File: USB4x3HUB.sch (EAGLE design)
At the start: 119 parts, among them IC1 TUSB2036, IC10 SN74LVC1G139DCTR, IC2 FSUSB74MPX, IC3 TPS2041C, IC4 TPS2041C, IC5 TPS2041C, IC6 3.3V, IC7 5V, IC8 5V, IC9 5V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

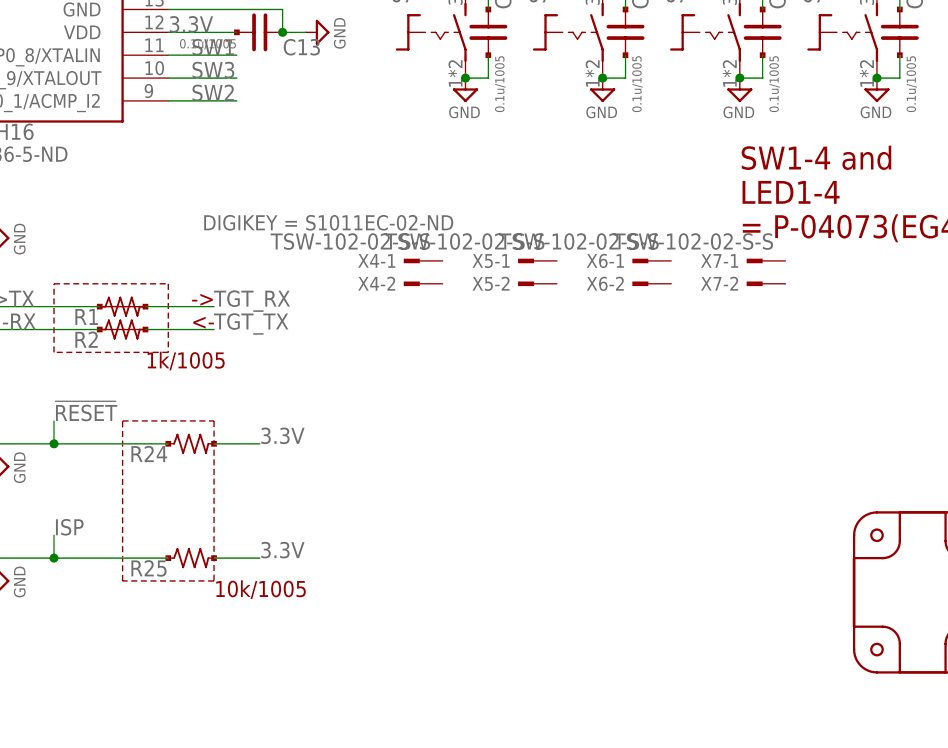
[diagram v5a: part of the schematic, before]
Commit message: [ BRD ] X4-7 pin1 connects to each switch inputs
- move SW1-4 silk
- move CON1-4 silk
- move X4-7 silk
- add 2.8mm hole for M2.6 screw
   - add tRestrict zone for it
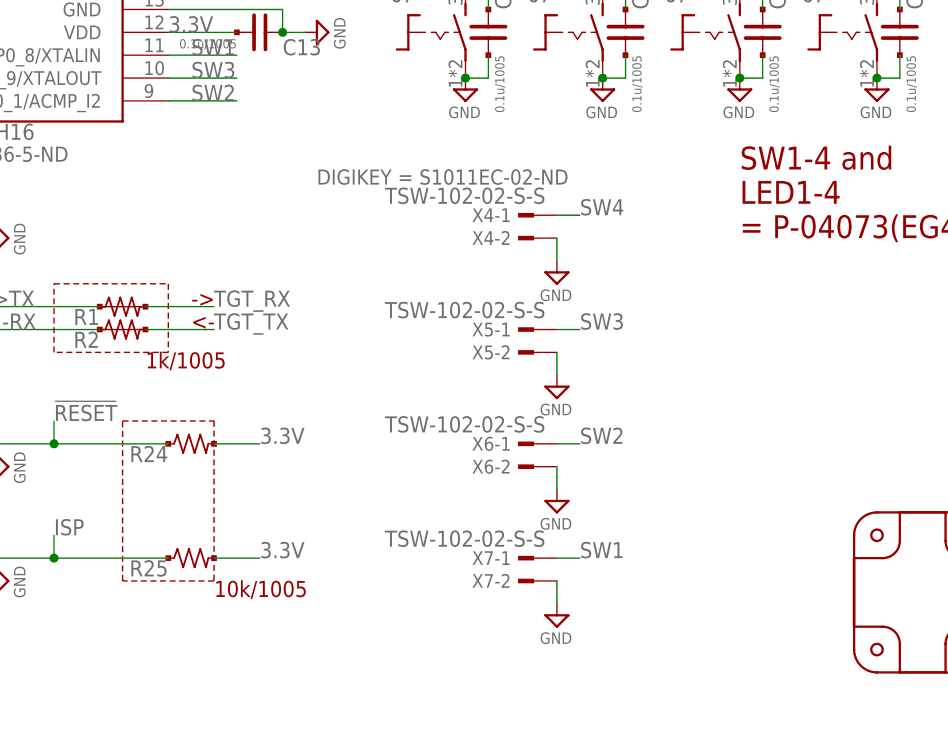
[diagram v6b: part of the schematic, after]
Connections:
- net GND: now also X4-2.1, X5-2.1, X6-2.1, X7-2.1
- net SW1: now also X7-1.1
- net SW2: now also X6-1.1
- net SW3: now also X5-1.1
- net SW4: now also X4-1.1
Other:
- moved on the sheet: X4-1, X4-2, X5-1, X5-2, X6-1, X6-2, X7-1, X7-2
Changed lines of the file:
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@@
 <part name="SW2" library="mylib" deviceset="TACTSW2_*" device="_SKRPACE010" technology="WH"/>
 <part name="SW1" library="mylib" deviceset="TACTSW2_*" device="_SKRPACE010" technology="WH"/>
+<part name="SUPPLY34" library="mylib" deviceset="GND" device=""/>
+<part name="SUPPLY42" library="mylib" deviceset="GND" device=""/>
+<part name="SUPPLY43" library="mylib" deviceset="GND" device=""/>
+<part name="SUPPLY44" library="mylib" deviceset="GND" device=""/>
 </parts>
 <sheets>
@@
 <instance part="P4" gate="G$1" x="251.46" y="10.16"/>
 <instance part="TP5" gate="1" x="165.1" y="157.48" rot="R180"/>
-<instance part="X4" gate="-1" x="193.04" y="50.8" rot="MR0">
-<attribute name="DIGIKEY" x="182.88" y="55.88" size="1.6764" layer="96" rot="MR180" align="bottom-center" display="both"/>
-</instance>
-<instance part="X4" gate="-2" x="193.04" y="48.26" rot="MR0"/>
-<instance part="X5" gate="-1" x="205.74" y="50.8" rot="MR0"/>
-<instance part="X5" gate="-2" x="205.74" y="48.26" rot="MR0"/>
-<instance part="X6" gate="-1" x="218.44" y="50.8" rot="MR0"/>
-<instance part="X6" gate="-2" x="218.44" y="48.26" rot="MR0"/>
-<instance part="X7" gate="-1" x="231.14" y="50.8" rot="MR0"/>
-<instance part="X7" gate="-2" x="231.14" y="48.26" rot="MR0"/>
+<instance part="X4" gate="-1" x="205.74" y="55.88" rot="MR0">
+<attribute name="DIGIKEY" x="195.58" y="60.96" size="1.6764" layer="96" rot="MR180" align="bottom-center" display="both"/>
+</instance>
+<instance part="X4" gate="-2" x="205.74" y="53.34" rot="MR0"/>
+<instance part="X5" gate="-1" x="205.74" y="43.18" rot="MR0"/>
+<instance part="X5" gate="-2" x="205.74" y="40.64" rot="MR0"/>
+<instance part="X6" gate="-1" x="205.74" y="30.48" rot="MR0"/>
+<instance part="X6" gate="-2" x="205.74" y="27.94" rot="MR0"/>
+<instance part="X7" gate="-1" x="205.74" y="17.78" rot="MR0"/>
+<instance part="X7" gate="-2" x="205.74" y="15.24" rot="MR0"/>
 <instance part="SW4" gate="G$1" x="195.58" y="76.2"/>
 <instance part="SW3" gate="G$1" x="210.82" y="76.2"/>
 <instance part="SW2" gate="G$1" x="226.06" y="76.2"/>
 <instance part="SW1" gate="G$1" x="241.3" y="76.2"/>
+<instance part="SUPPLY34" gate="GND" x="208.28" y="48.26"/>
+<instance part="SUPPLY42" gate="GND" x="208.28" y="35.56"/>
+<instance part="SUPPLY43" gate="GND" x="208.28" y="22.86"/>
+<instance part="SUPPLY44" gate="GND" x="208.28" y="10.16"/>
 </instances>
 <busses>
@@
 <pinref part="SUPPLY41" gate="GND" pin="GND"/>
 </segment>
+<segment>
+<pinref part="X4" gate="-2" pin="1"/>
+<pinref part="SUPPLY34" gate="GND" pin="GND"/>
+<wire x1="208.28" y1="50.8" x2="208.28" y2="53.34" width="0.1524" layer="91"/>
+</segment>
+<segment>
+<pinref part="X5" gate="-2" pin="1"/>
+<pinref part="SUPPLY42" gate="GND" pin="GND"/>
+<wire x1="208.28" y1="38.1" x2="208.28" y2="40.64" width="0.1524" layer="91"/>
+</segment>
+<segment>
+<pinref part="X6" gate="-2" pin="1"/>
+<pinref part="SUPPLY43" gate="GND" pin="GND"/>
+<wire x1="208.28" y1="25.4" x2="208.28" y2="27.94" width="0.1524" layer="91"/>
+</segment>
+<segment>
+<pinref part="X7" gate="-2" pin="1"/>
+<pinref part="SUPPLY44" gate="GND" pin="GND"/>
+<wire x1="208.28" y1="12.7" x2="208.28" y2="15.24" width="0.1524" layer="91"/>
+</segment>
 </net>
 <net name="3.3V" class="0">
@@
 <label x="167.64" y="73.66" size="1.778" layer="95"/>
 </segment>
+<segment>
+<wire x1="208.28" y1="17.78" x2="210.82" y2="17.78" width="0.1524" layer="91"/>
+<pinref part="X7" gate="-1" pin="1"/>
+<label x="210.82" y="17.78" size="1.778" layer="95"/>
+</segment>
 </net>
 <net name="SW2" class="0">
@@
 <label x="167.64" y="68.58" size="1.778" layer="95"/>
 </segment>
+<segment>
+<wire x1="208.28" y1="30.48" x2="210.82" y2="30.48" width="0.1524" layer="91"/>
+<pinref part="X6" gate="-1" pin="1"/>
+<label x="210.82" y="30.48" size="1.778" layer="95"/>
+</segment>
 </net>
 <net name="SW3" class="0">
@@
 <label x="167.64" y="71.12" size="1.778" layer="95"/>
 </segment>
+<segment>
+<wire x1="208.28" y1="43.18" x2="210.82" y2="43.18" width="0.1524" layer="91"/>
+<pinref part="X5" gate="-1" pin="1"/>
+<label x="210.82" y="43.18" size="1.778" layer="95"/>
+</segment>
 </net>
 <net name="SW4" class="0">
@@
 <label x="106.68" y="68.58" size="1.778" layer="95"/>
 </segment>
-</net>
+<segment>
+<wire x1="208.28" y1="55.88" x2="210.82" y2="55.88" width="0.1524" layer="91"/>
+<pinref part="X4" gate="-1" pin="1"/>
+<label x="210.82" y="55.88" size="1.778" layer="95"/>
+</segment>
+</net>

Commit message: [ PCB ] add sheet for daughter board; move M2.6 hole; library update
- prepare daughter board
- apply updated library and use TACTSW2 component
- more consideration required
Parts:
- added P5, P6, P7, P8: (no value), mylib:PCB_CORNER_NH
- added SW5, SW6, SW7, SW8: (no value), mylib:TACTSW2_BK_TL1105S
- added X10, X11, X8, X9: TSW-102-02-S-S, con-samtec.local:TSW-102-02-S-S
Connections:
- new net N$74: SW8.S, X8-2.1
- new net N$75: SW7.S, X9-2.1
- new net N$76: SW6.S, X10-2.1
- new net N$77: SW5.S, X11-2.1
- new net SW5: SW5.P, X11-1.1
- new net SW6: SW6.P, X10-1.1
- new net SW7: SW7.P, X9-1.1
- new net SW8: SW8.P, X8-1.1
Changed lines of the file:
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@@
 <part name="SUPPLY43" library="mylib" deviceset="GND" device=""/>
 <part name="SUPPLY44" library="mylib" deviceset="GND" device=""/>
+<part name="FRAME2" library="frames" deviceset="A3L-LOC" device=""/>
+<part name="P5" library="mylib" deviceset="PCB_CORNER" device="_NH"/>
+<part name="P6" library="mylib" deviceset="PCB_CORNER" device="_NH"/>
+<part name="P7" library="mylib" deviceset="PCB_CORNER" device="_NH"/>
+<part name="P8" library="mylib" deviceset="PCB_CORNER" device="_NH"/>
+<part name="X8" library="con-samtec.local" deviceset="TSW-102-02-S-S" device="" value="TSW-102-02-S-S">
+<attribute name="NOT_COMPONENT" value="YES"/>
+</part>
+<part name="X9" library="con-samtec.local" deviceset="TSW-102-02-S-S" device="" value="TSW-102-02-S-S">
+<attribute name="NOT_COMPONENT" value="YES"/>
+</part>
+<part name="X10" library="con-samtec.local" deviceset="TSW-102-02-S-S" device="" value="TSW-102-02-S-S">
+<attribute name="NOT_COMPONENT" value="YES"/>
+</part>
+<part name="X11" library="con-samtec.local" deviceset="TSW-102-02-S-S" device="" value="TSW-102-02-S-S">
+<attribute name="NOT_COMPONENT" value="YES"/>
+</part>
+<part name="SW5" library="mylib" deviceset="TACTSW2_*" device="_TL1105S" technology="BK"/>
+<part name="SW6" library="mylib" deviceset="TACTSW2_*" device="_TL1105S" technology="BK"/>
+<part name="SW7" library="mylib" deviceset="TACTSW2_*" device="_TL1105S" technology="BK"/>
+<part name="SW8" library="mylib" deviceset="TACTSW2_*" device="_TL1105S" technology="BK"/>
 </parts>
 <sheets>
 <sheet>
+<description>main</description>
 <plain>
 <text x="167.64" y="43.18" size="1.778" layer="94">&lt;-</text>
@@
 </segment>
 </net>
+</nets>
+</sheet>
+<sheet>
+<plain>
+<wire x1="271.78" y1="17.78" x2="271.78" y2="10.16" width="0.3048" layer="94"/>
+<wire x1="276.86" y1="5.08" x2="281.94" y2="5.08" width="0.3048" layer="94"/>
+<wire x1="287.02" y1="10.16" x2="287.02" y2="17.78" width="0.3048" layer="94"/>
+<wire x1="281.94" y1="22.86" x2="276.86" y2="22.86" width="0.3048" layer="94"/>
+</plain>
+<instances>
+<instance part="FRAME2" gate="G$1" x="0" y="0"/>
+<instance part="P5" gate="G$1" x="281.94" y="17.78" rot="R90"/>
+<instance part="P6" gate="G$1" x="276.86" y="17.78" rot="R180"/>
+<instance part="P7" gate="G$1" x="276.86" y="10.16" rot="R270"/>
+<instance part="P8" gate="G$1" x="281.94" y="10.16"/>
+<instance part="X8" gate="-1" x="109.22" y="144.78" rot="MR0">
+<attribute name="DIGIKEY" x="99.06" y="149.86" size="1.6764" layer="96" rot="MR180" align="bottom-center" display="both"/>
+</instance>
+<instance part="X8" gate="-2" x="147.32" y="144.78" rot="MR180"/>
+<instance part="X9" gate="-1" x="109.22" y="132.08" rot="MR0"/>
+<instance part="X9" gate="-2" x="147.32" y="132.08" rot="MR180"/>
+<instance part="X10" gate="-1" x="109.22" y="119.38" rot="MR0"/>
+<instance part="X10" gate="-2" x="147.32" y="119.38" rot="MR180"/>
+<instance part="X11" gate="-1" x="109.22" y="106.68" rot="MR0"/>
+<instance part="X11" gate="-2" x="147.32" y="106.68" rot="MR180"/>
+<instance part="SW5" gate="G$1" x="129.54" y="109.22" rot="R270"/>
+<instance part="SW6" gate="G$1" x="129.54" y="121.92" rot="R270"/>
+<instance part="SW7" gate="G$1" x="129.54" y="134.62" rot="R270"/>
+<instance part="SW8" gate="G$1" x="129.54" y="147.32" rot="R270"/>
+</instances>
+<busses>
+</busses>
+<nets>
+<net name="SW8" class="0">
+<segment>
+<wire x1="111.76" y1="144.78" x2="124.46" y2="144.78" width="0.1524" layer="91"/>
+<pinref part="X8" gate="-1" pin="1"/>
+<label x="114.3" y="144.78" size="1.778" layer="95"/>
+<pinref part="SW8" gate="G$1" pin="P"/>
+</segment>
+</net>
+<net name="SW7" class="0">
+<segment>
+<wire x1="111.76" y1="132.08" x2="124.46" y2="132.08" width="0.1524" layer="91"/>
+<pinref part="X9" gate="-1" pin="1"/>
+<label x="114.3" y="132.08" size="1.778" layer="95"/>
+<pinref part="SW7" gate="G$1" pin="P"/>
+</segment>
+</net>
+<net name="SW6" class="0">
+<segment>
+<wire x1="111.76" y1="119.38" x2="124.46" y2="119.38" width="0.1524" layer="91"/>
+<pinref part="X10" gate="-1" pin="1"/>
+<label x="114.3" y="119.38" size="1.778" layer="95"/>
+<pinref part="SW6" gate="G$1" pin="P"/>
+</segment>
+</net>
+<net name="SW5" class="0">
+<segment>
+<wire x1="111.76" y1="106.68" x2="124.46" y2="106.68" width="0.1524" layer="91"/>
+<pinref part="X11" gate="-1" pin="1"/>
+<label x="114.3" y="106.68" size="1.778" layer="95"/>
+<pinref part="SW5" gate="G$1" pin="P"/>
+</segment>
+</net>
+<net name="N$74" class="0">
+<segment>
+<pinref part="SW8" gate="G$1" pin="S"/>
+<pinref part="X8" gate="-2" pin="1"/>
+<wire x1="144.78" y1="144.78" x2="134.62" y2="144.78" width="0.1524" layer="91"/>
+</segment>
+</net>
+<net name="N$75" class="0">
+<segment>
+<pinref part="SW7" gate="G$1" pin="S"/>
+<pinref part="X9" gate="-2" pin="1"/>
+<wire x1="144.78" y1="132.08" x2="134.62" y2="132.08" width="0.1524" layer="91"/>
+</segment>
+</net>
+<net name="N$76" class="0">
+<segment>
+<pinref part="SW6" gate="G$1" pin="S"/>
+<pinref part="X10" gate="-2" pin="1"/>
+<wire x1="144.78" y1="119.38" x2="134.62" y2="119.38" width="0.1524" layer="91"/>
+</segment>
+</net>
+<net name="N$77" class="0">
+<segment>
+<pinref part="SW5" gate="G$1" pin="S"/>
+<pinref part="X11" gate="-2" pin="1"/>
+<wire x1="144.78" y1="106.68" x2="134.62" y2="106.68" width="0.1524" layer="91"/>
+</segment>
+</net>

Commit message: [ PCB ] update library; remove south M2.6 hole; update panel design to reflect design change
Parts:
- SW1, SW2, SW3, SW4: NOT_COMPONENT (none) -> YES
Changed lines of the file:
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@@
 <attribute name="NOT_COMPONENT" value="YES"/>
 </part>
-<part name="SW4" library="mylib" deviceset="TACTSW2_*" device="_SKRPACE010" technology="WH"/>
-<part name="SW3" library="mylib" deviceset="TACTSW2_*" device="_SKRPACE010" technology="WH"/>
-<part name="SW2" library="mylib" deviceset="TACTSW2_*" device="_SKRPACE010" technology="WH"/>
-<part name="SW1" library="mylib" deviceset="TACTSW2_*" device="_SKRPACE010" technology="WH"/>
+<part name="SW4" library="mylib" deviceset="TACTSW2_*" device="_SKRPACE010" technology="WH">
+<attribute name="NOT_COMPONENT" value="YES"/>
+</part>
+<part name="SW3" library="mylib" deviceset="TACTSW2_*" device="_SKRPACE010" technology="WH">
+<attribute name="NOT_COMPONENT" value="YES"/>
+</part>
+<part name="SW2" library="mylib" deviceset="TACTSW2_*" device="_SKRPACE010" technology="WH">
+<attribute name="NOT_COMPONENT" value="YES"/>
+</part>
+<part name="SW1" library="mylib" deviceset="TACTSW2_*" device="_SKRPACE010" technology="WH">
+<attribute name="NOT_COMPONENT" value="YES"/>
+</part>
 <part name="SUPPLY34" library="mylib" deviceset="GND" device=""/>
 <part name="SUPPLY42" library="mylib" deviceset="GND" device=""/>
@@
 <instance part="X7" gate="-1" x="205.74" y="17.78" rot="MR0"/>
 <instance part="X7" gate="-2" x="205.74" y="15.24" rot="MR0"/>
-<instance part="SW4" gate="G$1" x="195.58" y="76.2"/>
-<instance part="SW3" gate="G$1" x="210.82" y="76.2"/>
-<instance part="SW2" gate="G$1" x="226.06" y="76.2"/>
-<instance part="SW1" gate="G$1" x="241.3" y="76.2"/>
+<instance part="SW4" gate="G$1" x="195.58" y="76.2">
+<attribute name="NOT_COMPONENT" x="195.58" y="76.2" size="1.778" layer="96" display="off"/>
+</instance>
+<instance part="SW3" gate="G$1" x="210.82" y="76.2">
+<attribute name="NOT_COMPONENT" x="210.82" y="76.2" size="1.778" layer="96" display="off"/>
+</instance>
+<instance part="SW2" gate="G$1" x="226.06" y="76.2">
+<attribute name="NOT_COMPONENT" x="226.06" y="76.2" size="1.778" layer="96" display="off"/>
+</instance>
+<instance part="SW1" gate="G$1" x="241.3" y="76.2">
+<attribute name="NOT_COMPONENT" x="241.3" y="76.2" size="1.778" layer="96" display="off"/>
+</instance>
 <instance part="SUPPLY34" gate="GND" x="208.28" y="48.26"/>
 <instance part="SUPPLY42" gate="GND" x="208.28" y="35.56"/>
